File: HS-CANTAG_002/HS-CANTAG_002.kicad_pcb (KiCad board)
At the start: 2 copper layers, 100 x 60 mm, 27 parts, among them J1 5v_GND, J2 CAN_SPI, J3 AudioJack, J4 Debug_Serial, J5 Serial_5v, J6 i2c_3.3v, SW1 ID_DIP, U1 AE-ATMEGA328-MINI, U2 DFPLAYER_MINI, U3 R-783.3-0.5, U4 TWELITE_DIP

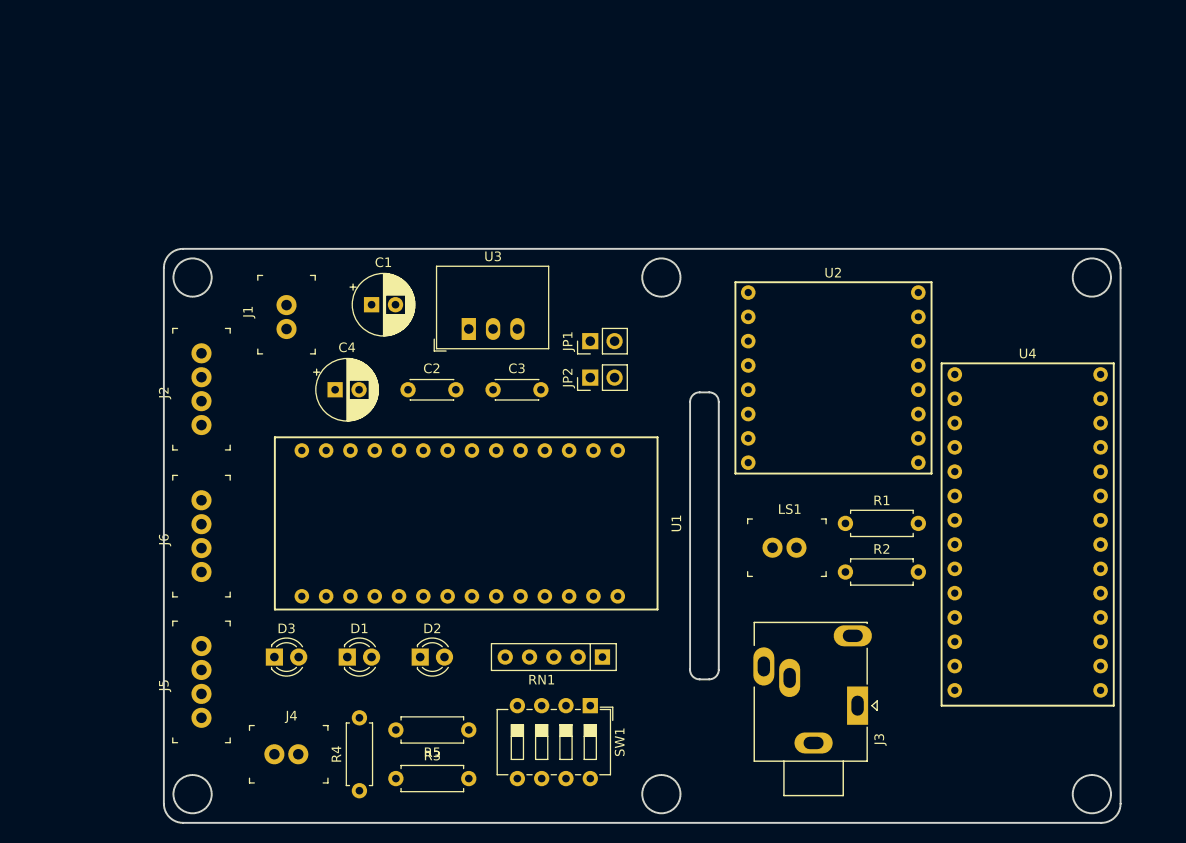
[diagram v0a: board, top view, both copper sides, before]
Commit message: ・CANTAG-002修正
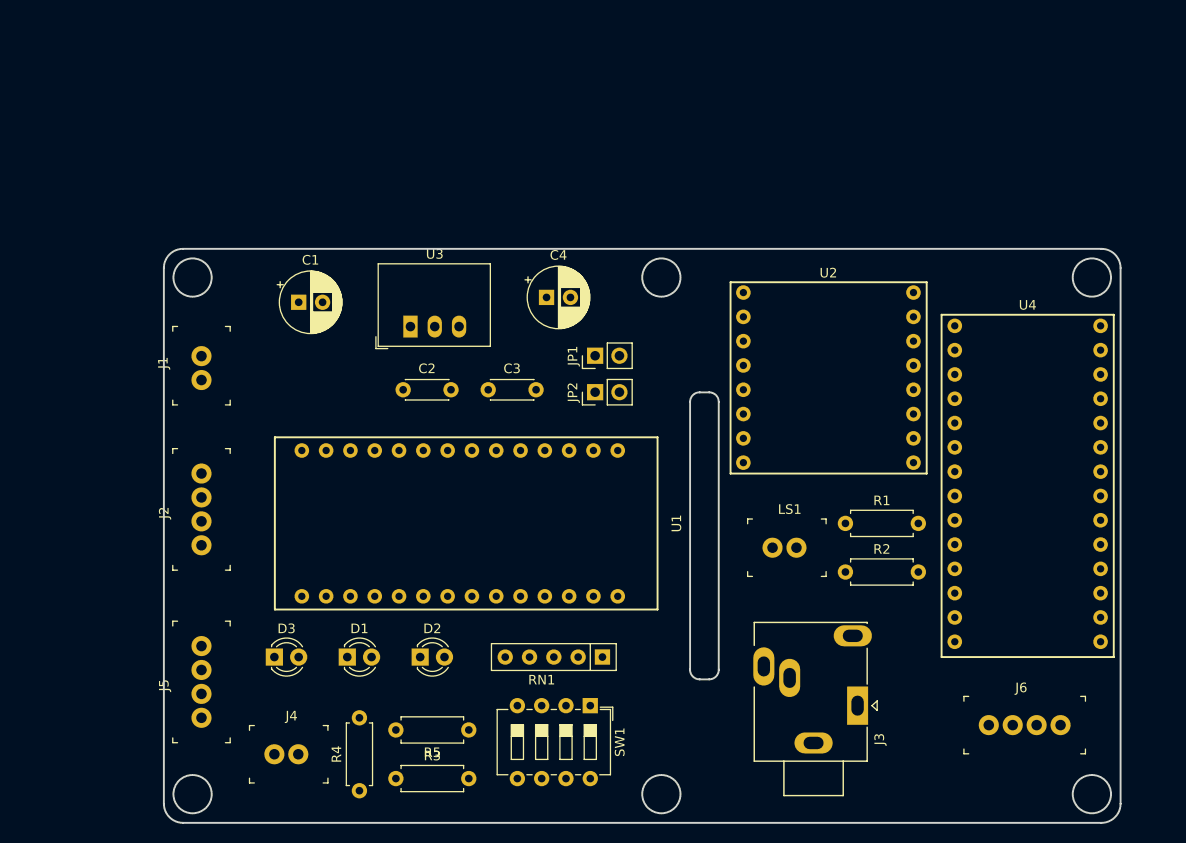
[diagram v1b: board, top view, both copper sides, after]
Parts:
- moved J6 83.8 mm to (181.4, 113.8), turned to 0 degrees
- moved C4 24.1 mm to (135.1, 69.1)
- moved J2 12.6 mm to (99.1, 95.0)
- moved J1 10.4 mm to (99.1, 77.7)
- moved C1 7.62 mm to (109.2, 69.6)
- moved U3 6.10 mm to (120.9, 72.1)
- moved U4 5.08 mm to (185.4, 88.9)
- moved JP1 1.61 mm to (140.2, 75.2)
- moved JP2 1.61 mm to (140.2, 79.0)
- moved C2 0.51 mm to (120.1, 78.7)
- moved C3 0.51 mm to (129.0, 78.7)
- moved U2 0.51 mm to (164.6, 77.5)
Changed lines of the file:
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@@
   )
   (module Capacitor_THT:CP_Radial_D6.3mm_P2.50mm (layer F.Cu)
-    (at 116.84 69.85)
+    (at 109.22 69.596)
     (descr "CP, Radial series, Radial, pin pitch=2.50mm, , diameter=6.3mm, Electrolytic Capacitor")
     (tags "CP Radial series Radial pin pitch 2.50mm  diameter 6.3mm Electrolytic Capacitor")
@@
   )
   (module Capacitor_THT:C_Disc_D4.3mm_W1.9mm_P5.00mm (layer F.Cu)
-    (at 120.65 78.74)
+    (at 120.142 78.74)
     (descr "C, Disc series, Radial, pin pitch=5.00mm, , diameter*width=4.3*1.9mm^2, Capacitor, http://www.vishay.com/docs/45233/krseries.pdf")
     (tags "C Disc series Radial pin pitch 5.00mm  diameter 4.3mm width 1.9mm Capacitor")
@@
   )
   (module Capacitor_THT:C_Disc_D4.3mm_W1.9mm_P5.00mm (layer F.Cu)
-    (at 129.54 78.74)
+    (at 129.032 78.74)
     (descr "C, Disc series, Radial, pin pitch=5.00mm, , diameter*width=4.3*1.9mm^2, Capacitor, http://www.vishay.com/docs/45233/krseries.pdf")
     (tags "C Disc series Radial pin pitch 5.00mm  diameter 4.3mm width 1.9mm Capacitor")
@@
   )
   (module Capacitor_THT:CP_Radial_D6.3mm_P2.50mm (layer F.Cu)
-    (at 113.03 78.74)
+    (at 135.128 69.088)
     (descr "CP, Radial series, Radial, pin pitch=2.50mm, , diameter=6.3mm, Electrolytic Capacitor")
     (tags "CP Radial series Radial pin pitch 2.50mm  diameter 6.3mm Electrolytic Capacitor")
@@
   )
   (module digikey-footprints:PinHeader_1x2_P2.5mm_Drill1.1mm (layer F.Cu)
-    (at 107.95 72.39 90)
+    (at 99.06 77.724 90)
     (descr http://www.jst-mfg.com/product/pdf/eng/eXH.pdf)
     (fp_text reference J1 (at 1.8 -4 90) (layer F.SilkS)
@@
   )
   (module digikey-footprints:PinHeader_1x4_P2.5mm_Drill1.1mm (layer F.Cu)
-    (at 99.06 82.43 90)
+    (at 99.06 94.996 90)
     (descr http://www.jst-mfg.com/product/pdf/eng/eXH.pdf)
     (fp_text reference J2 (at 3.4 -3.9 90) (layer F.SilkS)
@@
   )
   (module digikey-footprints:PinHeader_1x4_P2.5mm_Drill1.1mm (layer F.Cu)
-    (at 99.06 97.79 90)
+    (at 181.356 113.792)
     (descr http://www.jst-mfg.com/product/pdf/eng/eXH.pdf)
-    (fp_text reference J6 (at 3.4 -3.9 90) (layer F.SilkS)
-      (effects (font (size 1 1) (thickness 0.15)))
-    )
-    (fp_text value i2c_3.3v (at 3.3 4.3 90) (layer F.Fab)
+    (fp_text reference J6 (at 3.4 -3.9) (layer F.SilkS)
+      (effects (font (size 1 1) (thickness 0.15)))
+    )
+    (fp_text value i2c_3.3v (at 3.3 4.3) (layer F.Fab)
       (effects (font (size 1 1) (thickness 0.15)))
     )
@@
     (fp_line (start 9.95 -2.875) (end 9.95 2.875) (layer F.Fab) (width 0.1))
     (fp_line (start -2.45 2.875) (end 9.95 2.875) (layer F.Fab) (width 0.1))
-    (fp_text user %R (at 3.8 0 90) (layer F.Fab)
+    (fp_text user %R (at 3.8 0) (layer F.Fab)
       (effects (font (size 1 1) (thickness 0.15)))
     )
@@
     (fp_line (start -2.45 -2.875) (end 9.95 -2.875) (layer F.Fab) (width 0.1))
     (fp_line (start -2.45 -2.875) (end -2.45 2.875) (layer F.Fab) (width 0.1))
-    (pad 1 thru_hole circle (at 0 0 90) (size 2.1 2.1) (drill 1.1) (layers *.Cu *.Mask)
-      (net 71 GND))
-    (pad 2 thru_hole circle (at 2.5 0 90) (size 2.1 2.1) (drill 1.1) (layers *.Cu *.Mask)
+    (pad 1 thru_hole circle (at 0 0) (size 2.1 2.1) (drill 1.1) (layers *.Cu *.Mask)
+      (net 71 GND))
+    (pad 2 thru_hole circle (at 2.5 0) (size 2.1 2.1) (drill 1.1) (layers *.Cu *.Mask)
       (net 2 +3.3V))
-    (pad 3 thru_hole circle (at 5 0 90) (size 2.1 2.1) (drill 1.1) (layers *.Cu *.Mask)
+    (pad 3 thru_hole circle (at 5 0) (size 2.1 2.1) (drill 1.1) (layers *.Cu *.Mask)
       (net 16 SCL))
-    (pad 4 thru_hole circle (at 7.5 0 90) (size 2.1 2.1) (drill 1.1) (layers *.Cu *.Mask)
+    (pad 4 thru_hole circle (at 7.5 0) (size 2.1 2.1) (drill 1.1) (layers *.Cu *.Mask)
       (net 17 SDA))
   )
   (module Connector_PinHeader_2.54mm:PinHeader_1x02_P2.54mm_Vertical (layer F.Cu)
-    (at 139.7 73.66 90)
+    (at 140.208 75.184 90)
     (descr "Through hole straight pin header, 1x02, 2.54mm pitch, single row")
     (tags "Through hole pin header THT 1x02 2.54mm single row")
@@
   )
   (module Connector_PinHeader_2.54mm:PinHeader_1x02_P2.54mm_Vertical (layer F.Cu)
-    (at 139.7 77.47 90)
+    (at 140.208 78.994 90)
     (descr "Through hole straight pin header, 1x02, 2.54mm pitch, single row")
     (tags "Through hole pin header THT 1x02 2.54mm single row")
@@
   )
   (module hotsprings-footprints:DFPlayer-MINI (layer F.Cu)
-    (at 165.1 77.47)
+    (at 164.592 77.47)
     (fp_text reference U2 (at 0 -10.93) (layer F.SilkS)
       (effects (font (size 1 1) (thickness 0.15)))
@@
   )
   (module Converter_DCDC:Converter_DCDC_RECOM_R-78E-0.5_THT (layer F.Cu)
-    (at 127 72.39)
+    (at 120.904 72.136)
     (descr "DCDC-Converter, RECOM, RECOM_R-78E-0.5, SIP-3, pitch 2.54mm, package size 11.6x8.5x10.4mm^3, https://www.recom-power.com/pdf/Innoline/R-78Exx-0.5.pdf")
     (tags "dc-dc recom buck sip-3 pitch 2.54mm")
@@
   )
   (module hotsprings-footprints:TWELITE-DIP (layer F.Cu)
-    (at 185.42 93.98)
+    (at 185.42 88.9)
     (fp_text reference U4 (at 0 -19) (layer F.SilkS)
       (effects (font (size 1 1) (thickness 0.15)))

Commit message: ・CANTAG_002基盤概成
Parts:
- moved R5 17.6 mm to (109.9, 110.2), turned to 90 degrees
- moved R3 17.0 mm to (114.4, 103.1)
- moved D2 16.4 mm to (109.1, 96.5)
- moved JP2 15.0 mm to (134.7, 65.0)
- moved R4 13.8 mm to (122.0, 108.5), turned to 180 degrees
- moved D3 11.5 mm to (101.2, 96.5)
- moved R2 11.5 mm to (160.9, 87.6)
- moved RN1 11.5 mm to (135.5, 96.5)
- moved J1 11.5 mm to (93.6, 67.6)
- moved C3 11.5 mm to (123.6, 68.6)
- moved J4 11.5 mm to (101.2, 106.7)
- moved LS1 11.5 mm to (153.3, 85.1)
- moved R1 11.5 mm to (160.9, 82.5)
- moved U2 11.5 mm to (159.1, 67.3)
- moved C1 11.5 mm to (103.8, 59.4)
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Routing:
- net +5V: track 0.00 -> 173.5 mm, vias 0 -> 1
- net +3.3V: track 0.00 -> 133.2 mm
- net RX_H: track 0.00 -> 111.1 mm
- net TX_H: track 0.00 -> 102.9 mm, vias 0 -> 1
- net SCL: track 0.00 -> 94.0 mm, vias 0 -> 1
- net SDA: track 0.00 -> 93.6 mm, vias 0 -> 1
- net Net-(JP2-Pad2): track 0.00 -> 75.5 mm
- net Net-(R1-Pad1): track 0.00 -> 68.5 mm
- net Net-(JP1-Pad2): track 0.00 -> 62.8 mm
- net Net-(J3-PadT): track 0.00 -> 46.1 mm, vias 0 -> 1
- net Net-(J3-PadR): track 0.00 -> 35.3 mm
- net Net-(R1-Pad2): track 0.00 -> 33.2 mm
- net Net-(U1-Pad3): track 0.00 -> 32.0 mm
- net CS: track 0.00 -> 25.2 mm
- net Net-(R2-Pad2): track 0.00 -> 22.9 mm
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- added copper zone on B.Cu, net GND
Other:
- board text added: "HS-CANTAG_002"

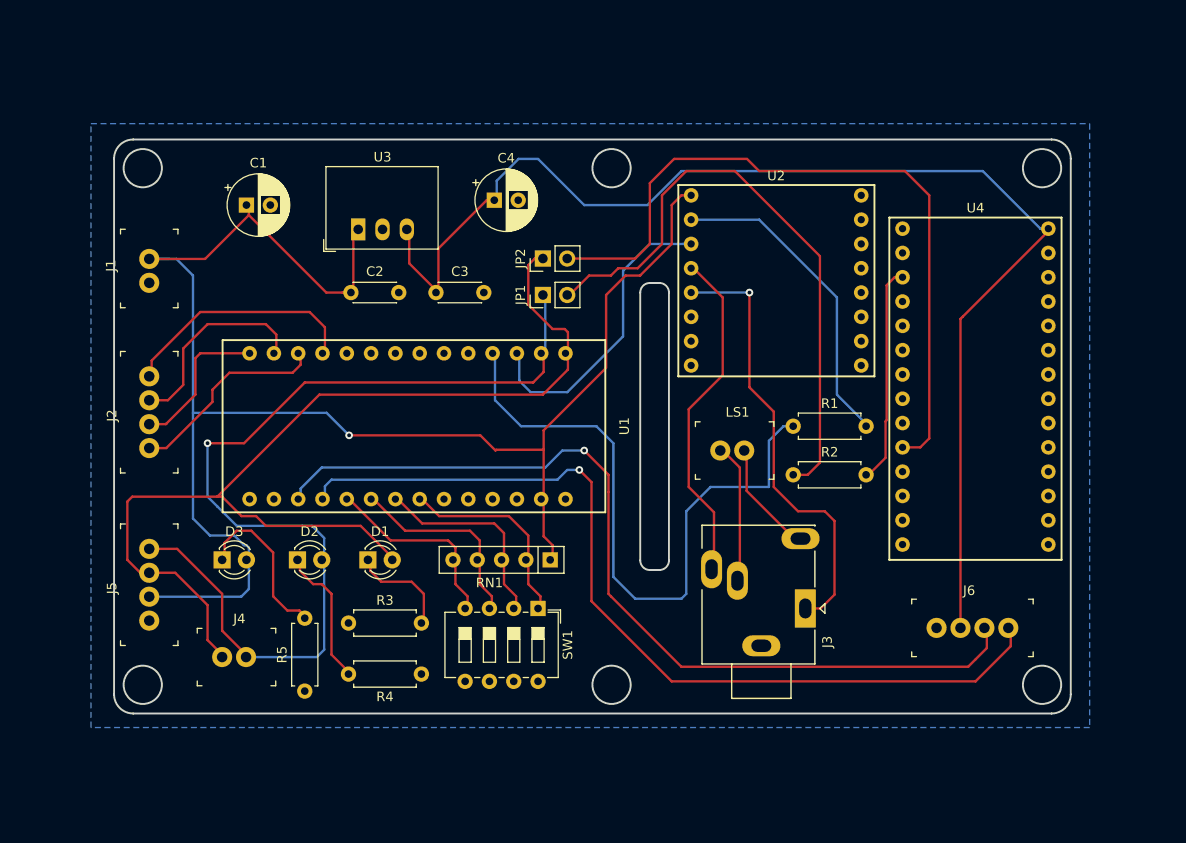
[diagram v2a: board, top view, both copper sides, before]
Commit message: ・CANTAG001外形変更 ・CANTAG002基盤修正
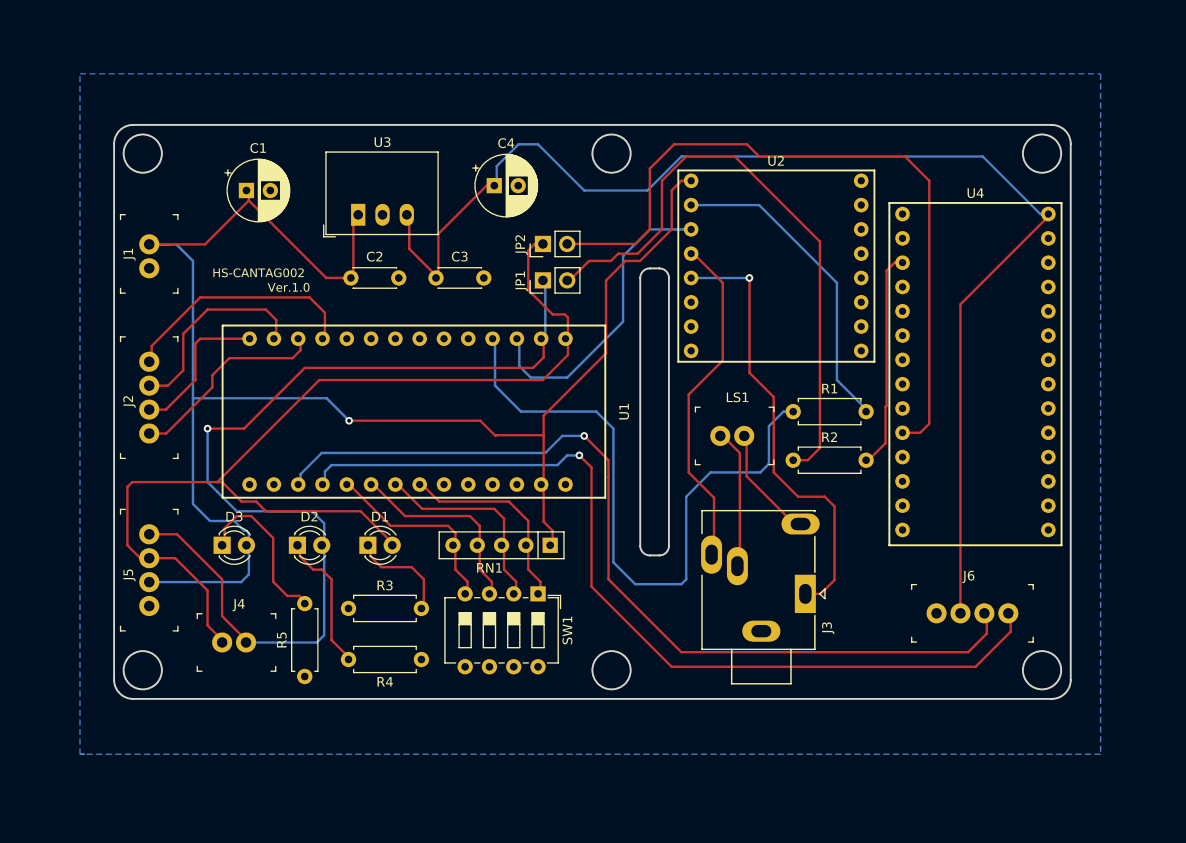
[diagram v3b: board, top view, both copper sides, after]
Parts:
- moved C1 1.52 mm to (103.8, 57.9)
- moved C2 1.52 mm to (114.7, 67.1)
- moved C3 1.52 mm to (123.6, 67.1)
- moved D1 1.52 mm to (116.5, 95.0)
- moved D2 1.52 mm to (109.1, 95.0)
- moved D3 1.52 mm to (101.2, 95.0)
- moved J2 1.52 mm to (93.6, 83.3)
- moved J3 1.52 mm to (162.2, 100.1)
- moved J4 1.52 mm to (101.2, 105.2)
- moved J5 1.52 mm to (93.6, 101.3)
- moved J6 1.52 mm to (175.9, 102.1)
- moved JP1 1.52 mm to (134.7, 67.3)
- moved JP2 1.52 mm to (134.7, 63.5)
- moved LS1 1.52 mm to (153.3, 83.6)
- moved R1 1.52 mm to (160.9, 81.0)
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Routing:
- net Net-(R1-Pad1): track 68.5 -> 67.9 mm
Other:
- board text added: "HS-CANTAG002"
- board text added: "Ver.1.0"
- board text removed: "HS-CANTAG_002"

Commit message: ・CANTAG002更新
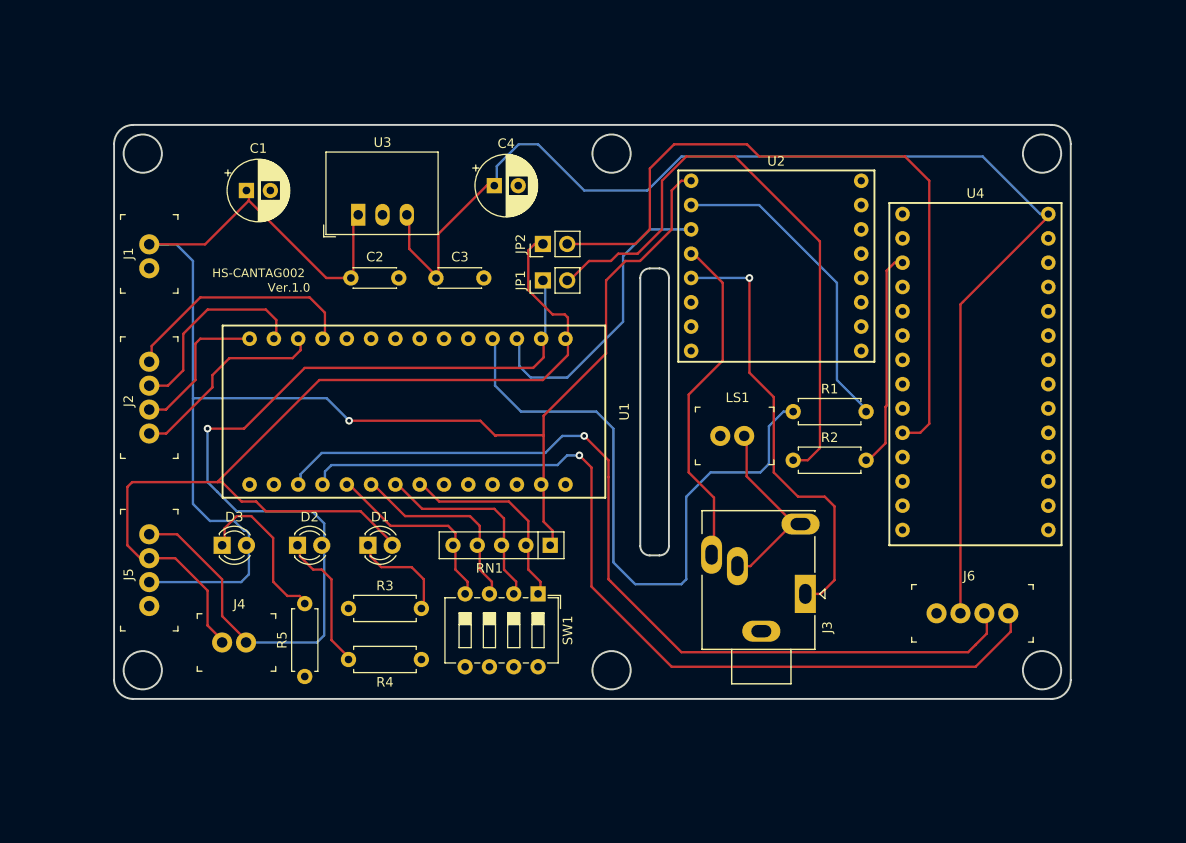
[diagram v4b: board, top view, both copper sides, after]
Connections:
- J3 pad TN: Net-(J3-PadTN) -> Net-(J3-PadRN)
- LS1 pad 1: Net-(J3-PadRN) -> GND
- LS1 pad 2: Net-(J3-PadTN) -> Net-(J3-PadRN)
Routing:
- net Net-(J3-PadTN): track 12.2 -> 0.00 mm
- net Net-(J3-PadRN): track 14.4 -> 20.6 mm
- removed copper zone on B.Cu, net GND

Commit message: ・各基盤修正
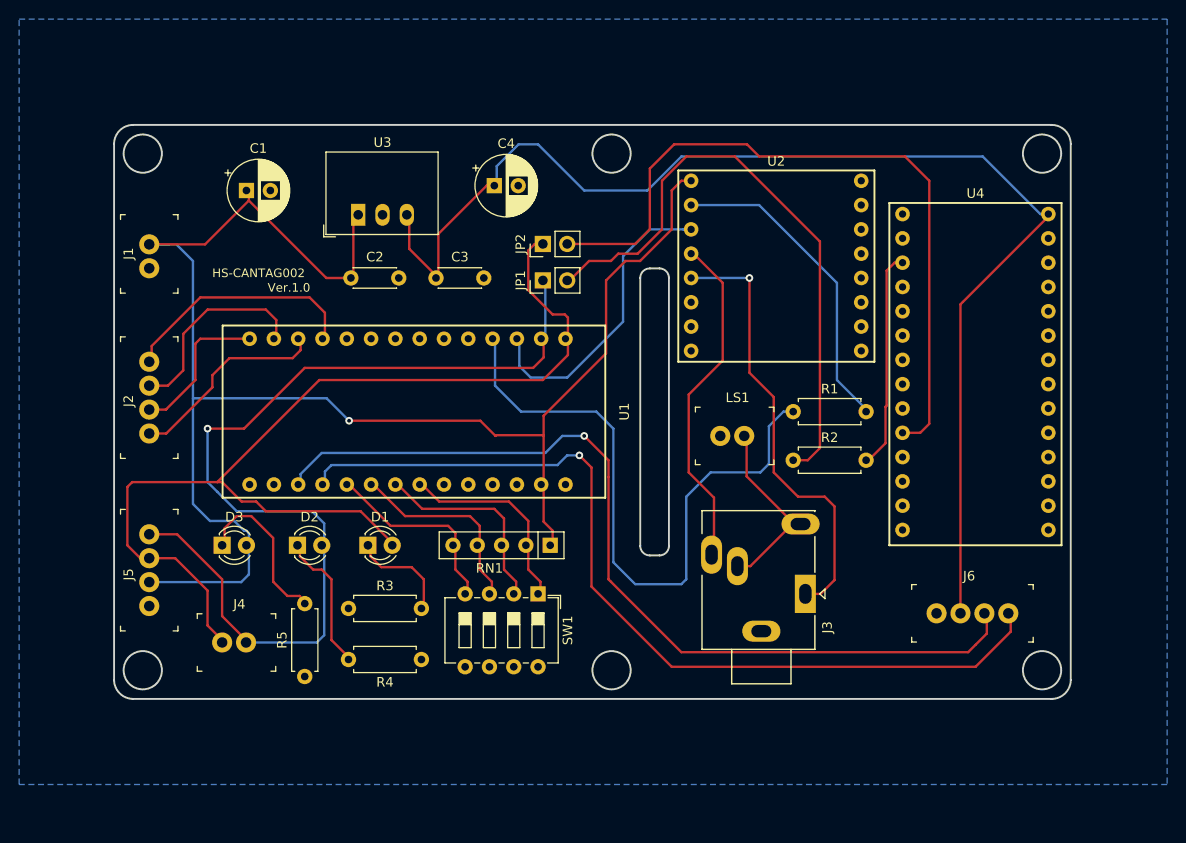
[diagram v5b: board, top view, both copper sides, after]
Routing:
- added copper zone on B.Cu, net GND
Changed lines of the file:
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@@
-(kicad_pcb (version 20171130) (host pcbnew "(5.1.2-1)-1")
+(kicad_pcb (version 20171130) (host pcbnew "(5.1.2)-2")
   (general
     (thickness 1.6)
@@
     (visible_elements 7FFFFFFF)
     (pcbplotparams
-      (layerselection 0x010fc_ffffffff)
-      (usegerberextensions false)
+      (layerselection 0x090fc_ffffffff)
+      (usegerberextensions true)
       (usegerberattributes false)
       (usegerberadvancedattributes false)
@@
       (outputformat 1)
       (mirror false)
-      (drillshape 1)
+      (drillshape 0)
       (scaleselection 1)
-      (outputdirectory ""))
+      (outputdirectory "C:/Users/YUUTA ISHII/Desktop/HS-CANTAG002/"))
   )
   (net 0 "")
@@
   (segment (start 132.283 76.276) (end 133.477 77.47) (width 0.25) (layer B.Cu) (net 26))
   (segment (start 143.129 71.628) (end 143.129 64.77) (width 0.25) (layer B.Cu) (net 26))
+  (zone (net 70) (net_name GND) (layer B.Cu) (hatch edge 0.508)
+    (connect_pads (clearance 0.508))
+    (min_thickness 0.254)
+    (fill yes (arc_segments 32) (thermal_gap 0.508) (thermal_bridge_width 0.508))
+    (polygon
+      (pts
+        (xy 80 40) (xy 200 40) (xy 200 120) (xy 80 120)
+      )
+    )
+  )
 )
